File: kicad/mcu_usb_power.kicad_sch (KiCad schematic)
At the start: 7 parts, among them J4 USB_B_Micro, U16 PCMF3USB3S, U5 MCXN947VDFT

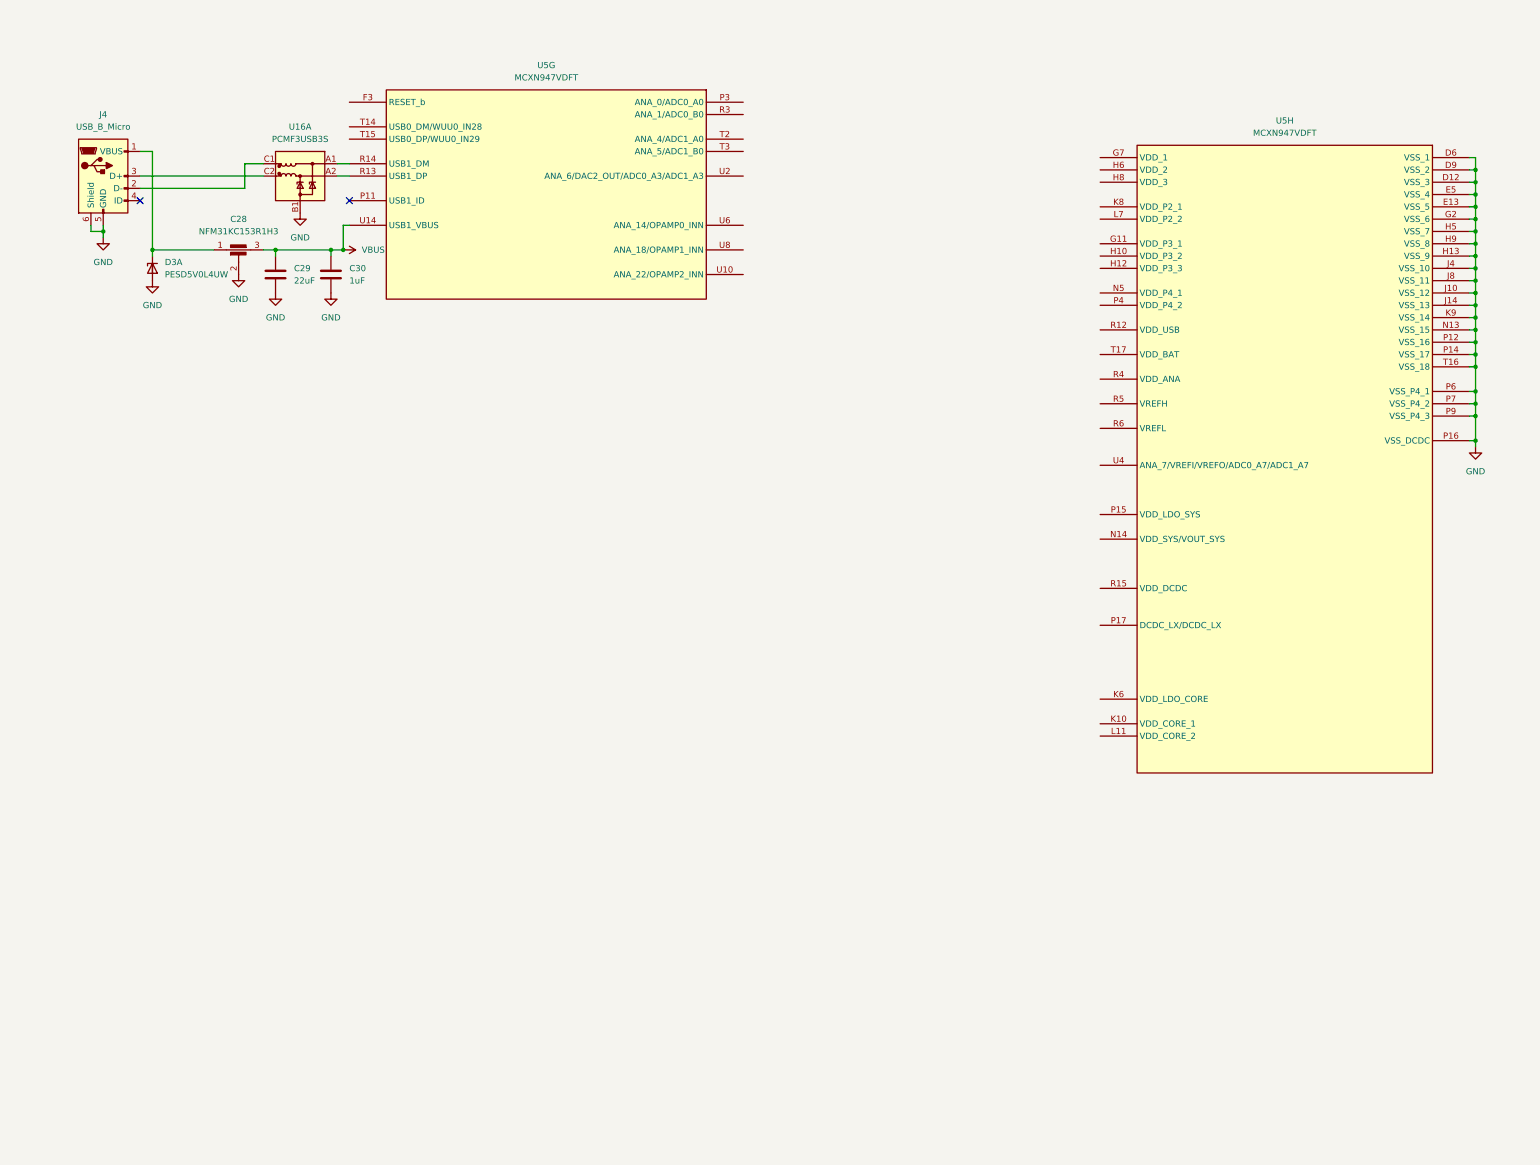
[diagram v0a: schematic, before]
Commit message: Updated schematics and BOM.
- Finished power supply schematics
- Added power schematic around MCXN
- Assigned MCXN pins
- Created board-to-board schematic and assigned pins to DF40T board-to-board connector
- Added correct sensors, finished sensor schematic
- Updated parts in communication schematic
- Added all part numbers etc in parts parameters
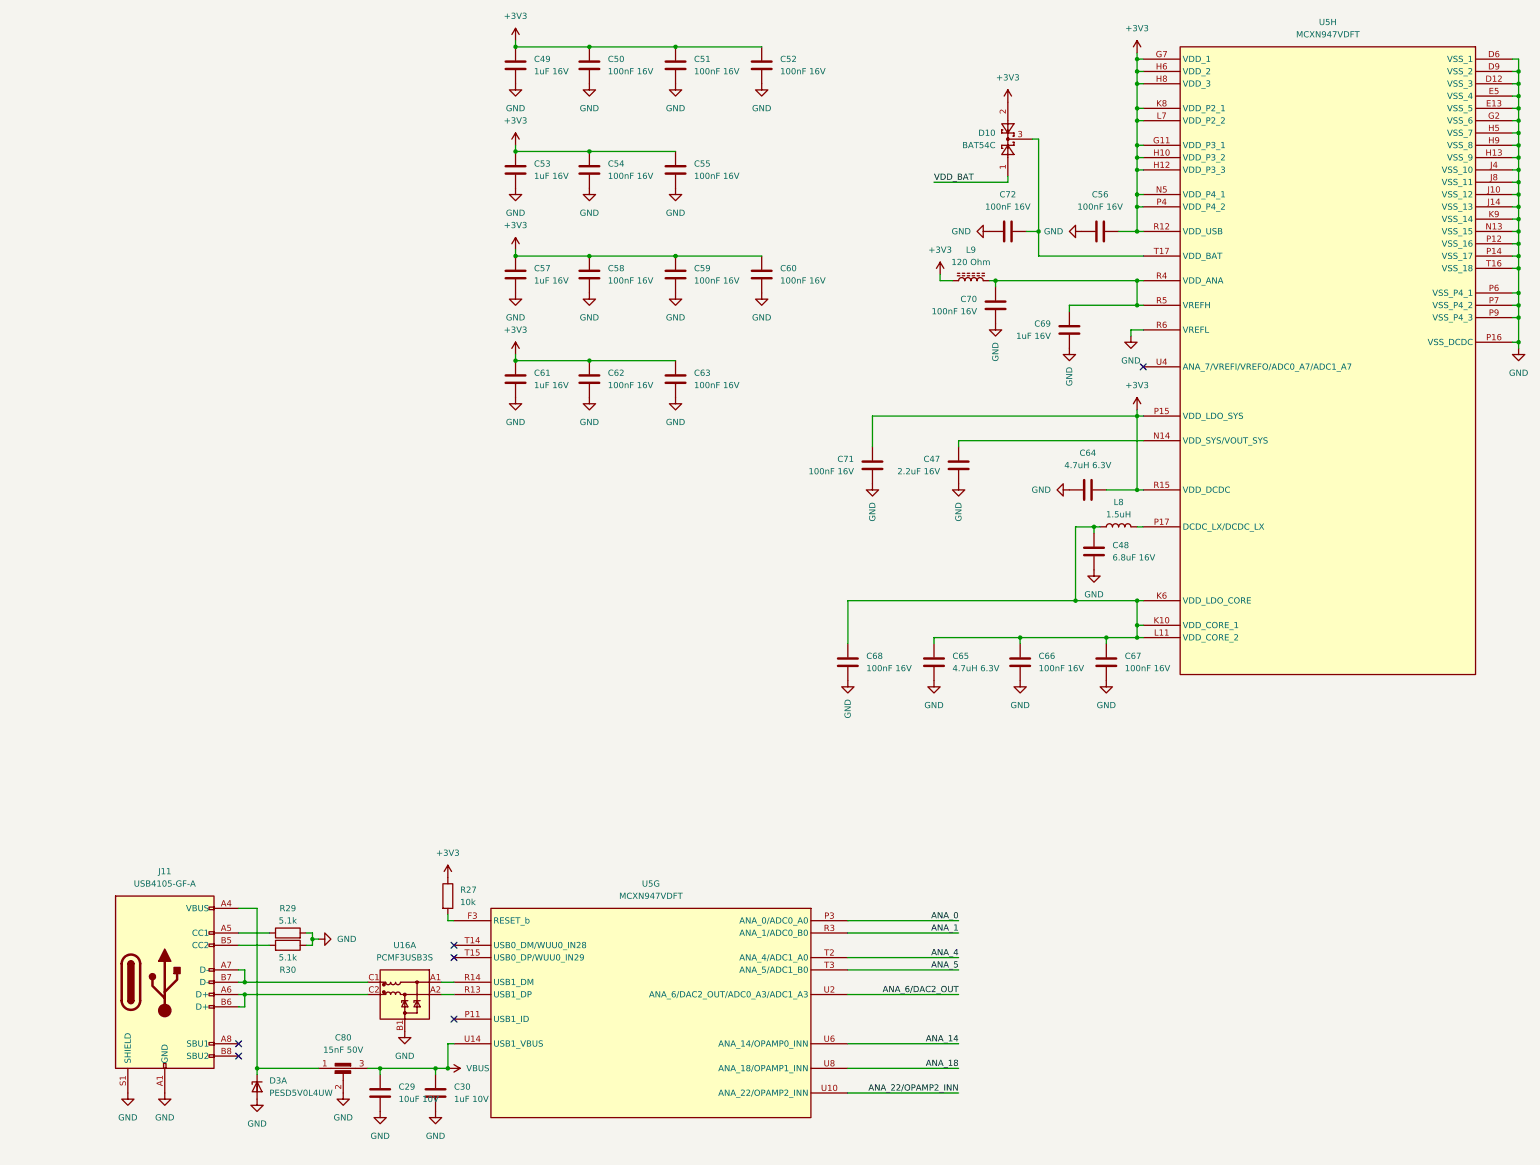
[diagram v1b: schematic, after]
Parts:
- removed C28: NFM31KC153R1H3, symbol Device:C_Feedthrough
- removed J4: USB_B_Micro, symbol Connector:USB_B_Micro
- added C47: 2.2uF 16V, Capacitor_SMD:C_0805_2012Metric, symbol Device:C
- added C48: 6.8uF 16V, Capacitor_SMD:C_1206_3216Metric, symbol Device:C
- added C49, C53, C57, C61, C69: 1uF 16V, Capacitor_SMD:C_0603_1608Metric, symbol Device:C
- added C50, C51, C52, C54, C55, C56, C58, C59, C60, C62, C63, C66, C67, C68, C70, C71, C72: 100nF 16V, Capacitor_SMD:C_0402_1005Metric, symbol Device:C
- added C64, C65: 4.7uH 6.3V, Capacitor_SMD:C_0603_1608Metric, symbol Device:C
- added C80: 15nF 50V, Capacitors:NFM31HK103R1H3L, symbol Capacitors:NFM31KC153R1H3L
- added D10: BAT54C, Package_TO_SOT_SMD:SOT-23, symbol Diode:BAT54C
- added J11: USB4105-GF-A, Connector_USB:USB_C_Receptacle_GCT_USB4105-xx-A_16P_TopMnt_Horizontal, symbol Connector:USB_C_Receptacle_USB2.0_16P
- added L8: 1.5uH, Inductor_SMD:L_1008_2520Metric, symbol Device:L
- added L9: 120 Ohm, Inductor_SMD:L_0402_1005Metric, symbol Device:L_Ferrite
- added R27: 10k, Resistor_SMD:R_0402_1005Metric, symbol Device:R
- added R29, R30: 5.1k, Resistor_SMD:R_0402_1005Metric, symbol Device:R
- C29: value 22uF -> 10uF 10V; footprint (none) -> Capacitor_SMD:C_0805_2012Metric; MF (none) -> Samsung Electro-Mechanics; MFPN (none) -> CL21B106KOQNNNE; Supplier (none) -> JLCPCB; Supplier PN (none) -> C95841
- C30: value 1uF -> 1uF 10V; footprint (none) -> Capacitor_SMD:C_0603_1608Metric; MF (none) -> Samsung Electro-Mechanics; MFPN (none) -> CL10B105KA8NNNC; Supplier (none) -> JLCPCB; Supplier PN (none) -> C29936
- D3: MF (none) -> TECH PUBLIC; MFPN (none) -> PESD5V0L4UW; Supplier (none) -> JLCPCB; Supplier PN (none) -> C2987081
- U16: MF (none) -> Nexperia USA Inc.; MFPN (none) -> PCMF3USB3SZ; Supplier (none) -> DigiKey; Supplier PN (none) -> 1727-2510-1-ND
- U5: MF (none) -> NXP USA Inc.; MFPN (none) -> MCXN947VDFT; Supplier (none) -> DigiKey; Supplier PN (none) -> 568-MCXN947VDFT-ND
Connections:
- net GND: now also U5.R6 (VREFL), C47.2, C48.2, C49.2, C50.2, C51.2, C52.2, C53.2, C54.2, C55.2, C56.1, C57.2, C58.2, C59.2, C60.2, C61.2, C62.2, C63.2, C64.2, C65.2, C66.2, C67.2, C68.1, C69.1, C70.1, C71.1, C72.1, C80.2, C80.4 (2), J11.A1 (GND), J11.A12 (GND), J11.B1 (GND), J11.B12 (GND), J11.S1 (SHIELD), R29.2, R30.1
- net VBUS: now also C80.3
- net at D3.1 (K1): now also C80.1, J11.A4 (VBUS), J11.A9 (VBUS), J11.B4 (VBUS), J11.B9 (VBUS)
- net at U16.C1 (CH1_OUT+): now also J11.A7 (D-), J11.B7 (D-)
- net at U16.C2 (CH1_OUT-): now also J11.A6 (D+), J11.B6 (D+)
- net +3V3: now reaches U5.G11 (VDD_P3_1)
- net +3V3: now also U5.G7 (VDD_1), U5.H10 (VDD_P3_2), U5.H12 (VDD_P3_3), U5.H6 (VDD_2), U5.H8 (VDD_3), U5.K8 (VDD_P2_1), U5.L7 (VDD_P2_2), U5.N5 (VDD_P4_1), U5.P15 (VDD_LDO_SYS), U5.P4 (VDD_P4_2), U5.R12 (VDD_USB), U5.R15 (VDD_DCDC), C49.1, C50.1, C51.1, C52.1, C53.1, C54.1, C55.1, C56.2, C57.1, C58.1, C59.1, C60.1, C61.1, C62.1, C63.1, C64.1, C71.2, D10.2, L9.1, R27.1
- net at U5.K10 (VDD_CORE_1): now also U5.K6 (VDD_LDO_CORE), U5.L11 (VDD_CORE_2), C48.1, C65.1, C66.1, C67.1, C68.2, L8.1
- net at U5.N14 (VDD_SYS/VOUT_SYS): now also C47.1
- net at U5.P17 (DCDC_LX/DCDC_LX): now also L8.2
- net at U5.R4 (VDD_ANA): now also U5.R5 (VREFH), C69.2, C70.2, L9.2
- net at U5.T17 (VDD_BAT): now also C72.2, D10.3
- net at U5.F3 (RESET_b): now also R27.2
- net ANA_0: now reaches U5.P3 (ANA_0/ADC0_A0)
- net ANA_1: now reaches U5.R3 (ANA_1/ADC0_B0)
- net ANA_4: now reaches U5.T2 (ANA_4/ADC1_A0)
- net ANA_5: now reaches U5.T3 (ANA_5/ADC1_B0)
- net ANA_22/OPAMP2_INN: now reaches U5.U10 (ANA_22/OPAMP2_INN)
- net ANA_6/DAC2_OUT: now reaches U5.U2 (ANA_6/DAC2_OUT/ADC0_A3/ADC1_A3)
- net ANA_14: now reaches U5.U6 (ANA_14/OPAMP0_INN)
- net ANA_18: now reaches U5.U8 (ANA_18/OPAMP1_INN)
- new net: J11.A5 (CC1), R29.1
- new net: J11.B5 (CC2), R30.2
- new net VDD_BAT: D10.1
- no-connect marks 2 -> 6
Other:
- moved on the sheet: C29, C30, D3A, U16A, U5G, U5H

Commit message: Finished schematic design for first review
Finished schematic design for first review.
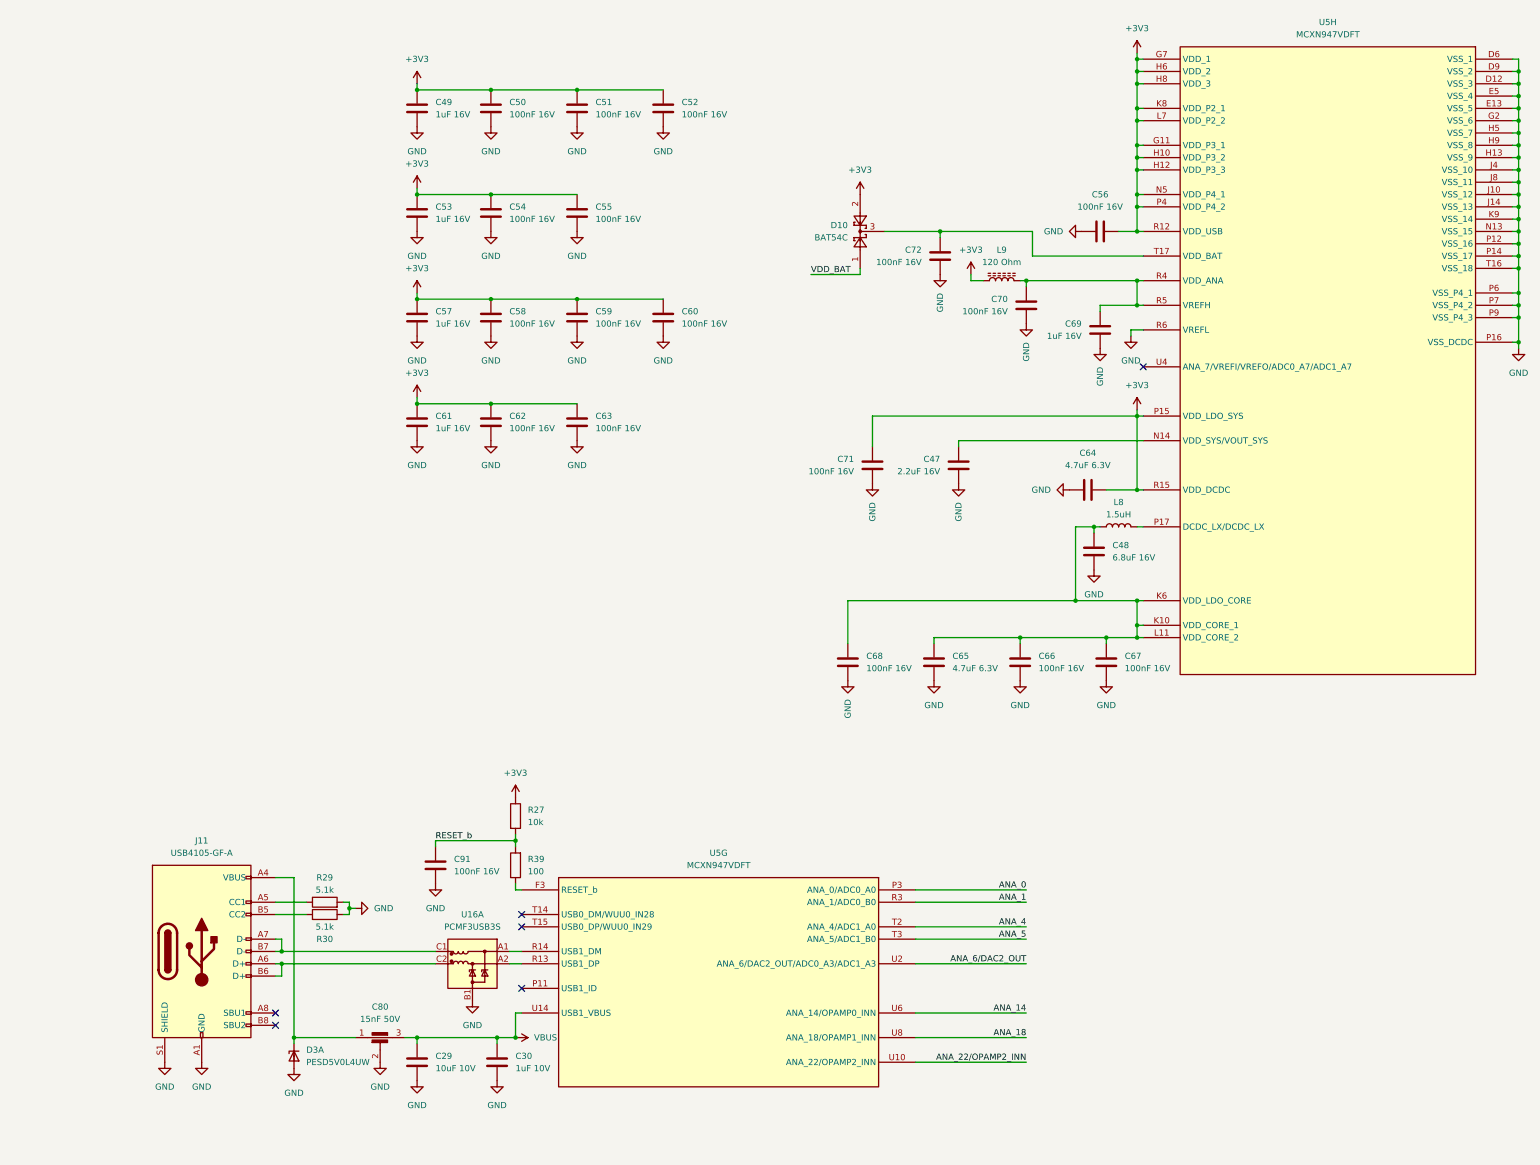
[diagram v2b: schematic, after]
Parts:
- added C91: 100nF 16V, Capacitor_SMD:C_0402_1005Metric, symbol Device:C
- added R39: 100, Resistor_SMD:R_0603_1608Metric, symbol Device:R
- C64, C65: value 4.7uH 6.3V -> 4.7uF 6.3V
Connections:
- net GND: now also C91.2
- net at U5.F3 (RESET_b): now also R39.1; no longer R27.2
- new net RESET_b: C91.1, R27.2, R39.2
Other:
- moved on the sheet: C29, C30, C49, C50, C51, C52, C53, C54, C55, C57, C58, C59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
